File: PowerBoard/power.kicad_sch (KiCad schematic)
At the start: 1 part, among them U3 NCV1117DT33T5G

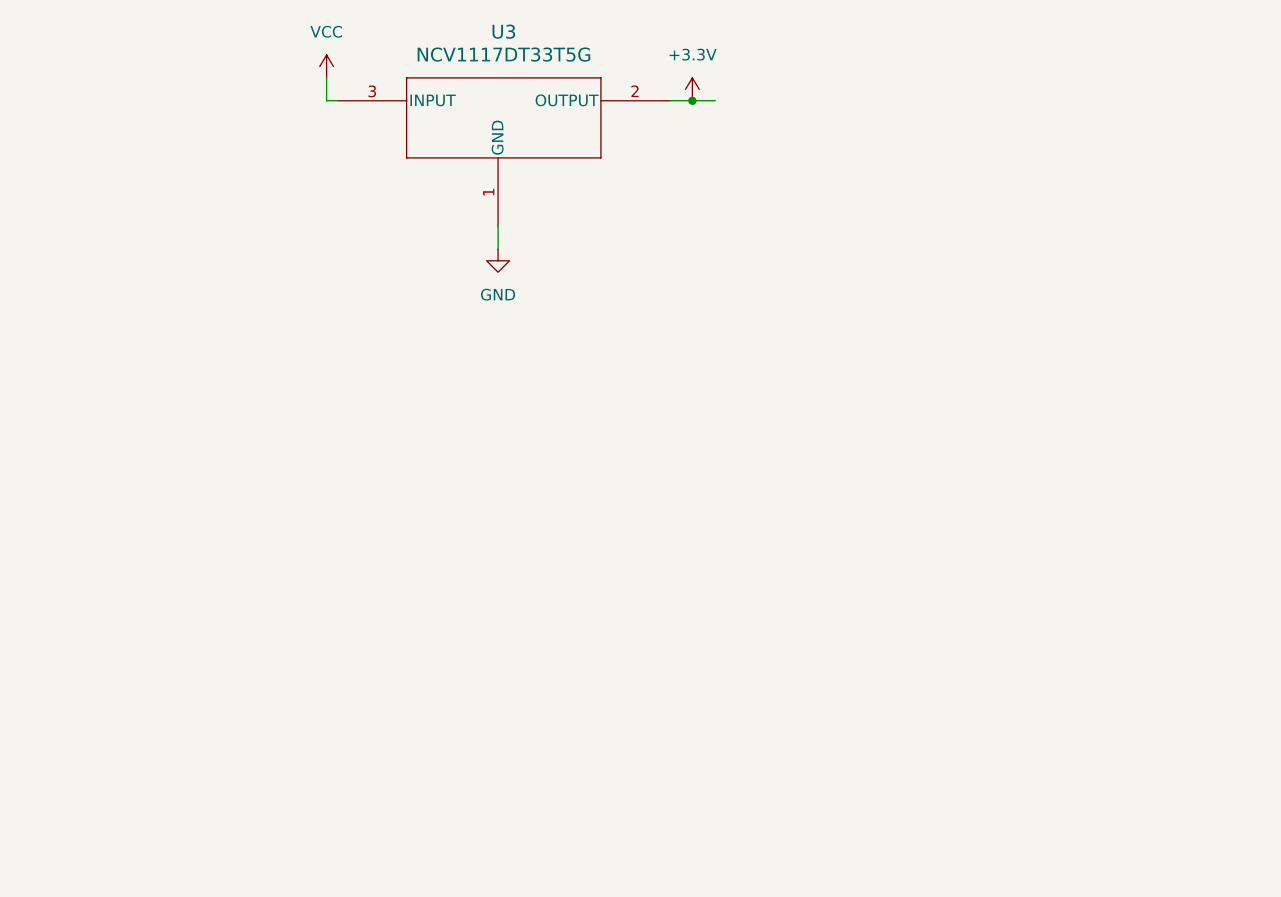
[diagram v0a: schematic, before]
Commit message: added 2040 flashing circuit and battery monitor
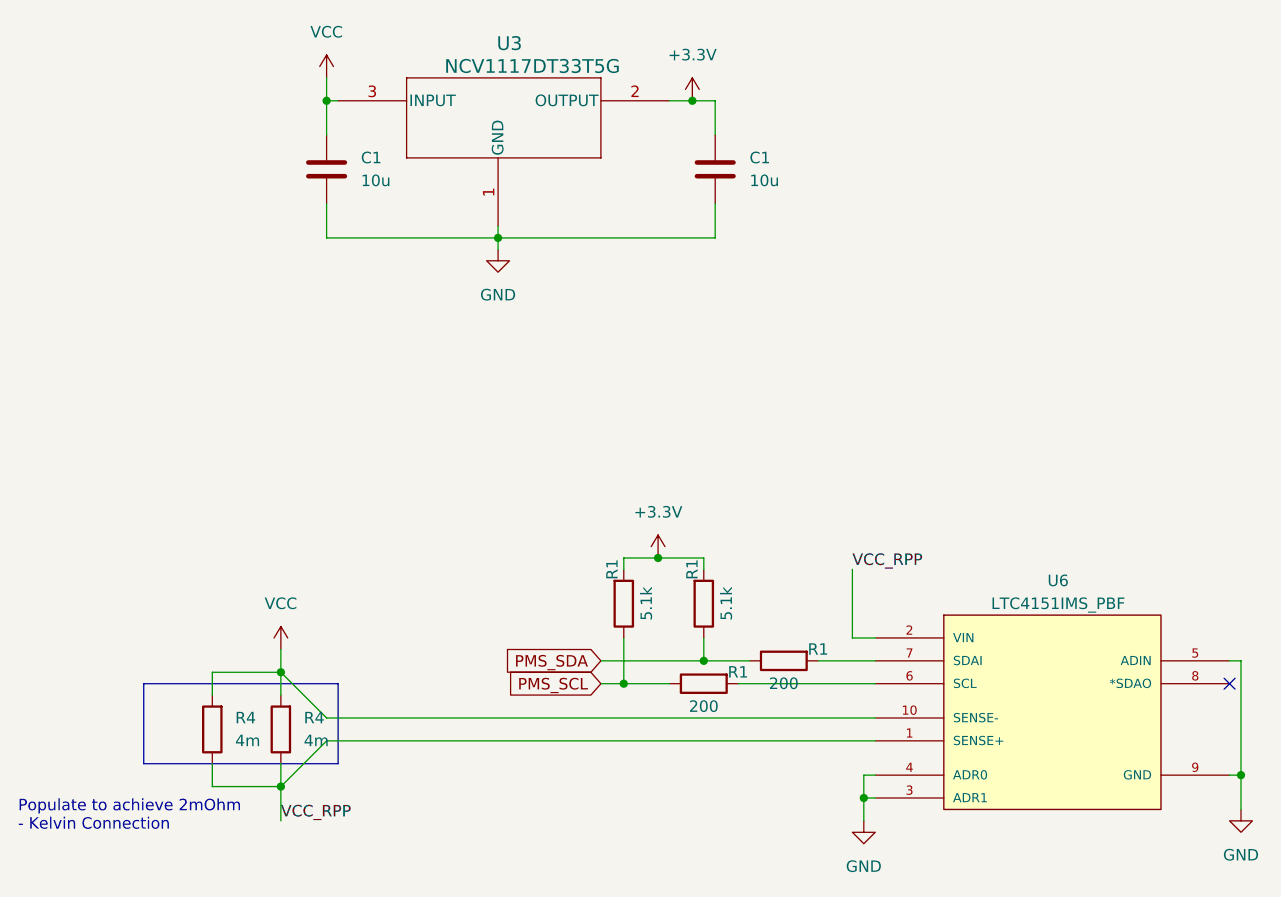
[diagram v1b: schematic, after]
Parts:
- added C1 (x2): 10u, Capacitor_SMD:C_0805_2012Metric, symbol Device:C
- added R1 (x2): 5.1k, Resistor_SMD:R_0603_1608Metric, symbol Device:R
- added R1 (x2): 200, Resistor_SMD:R_0603_1608Metric, symbol Device:R
- added R4 (x2): 4m, Resistor_SMD:R_1206_3216Metric, symbol Device:R
- added U6: LTC4151IMS_PBF, LTC4151IMS_PBF:MSOP-10_MS, symbol bots:LTC4151IMS_PBF
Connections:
- net +3.3V: now also C1.1, R1.2, R1.2
- net GND: now also C1.2, C1.2, U6.3 (ADR1), U6.4 (ADR0), U6.5 (ADIN), U6.9 (GND)
- net VCC: now also C1.1, R4.2, R4.2, U6.10 (SENSE-)
- new net: R1.2, U6.6 (SCL)
- new net: R1.2, U6.7 (SDAI)
- new net PMS_SCL: R1.1, R1.1
- new net PMS_SDA: R1.1, R1.1
- new net VCC_RPP: R4.1, R4.1, U6.1 (SENSE+), U6.2 (VIN)
- no-connect marks 0 -> 1
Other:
- note added: "Populate to achieve 2mOhm - Kelvin Connection"

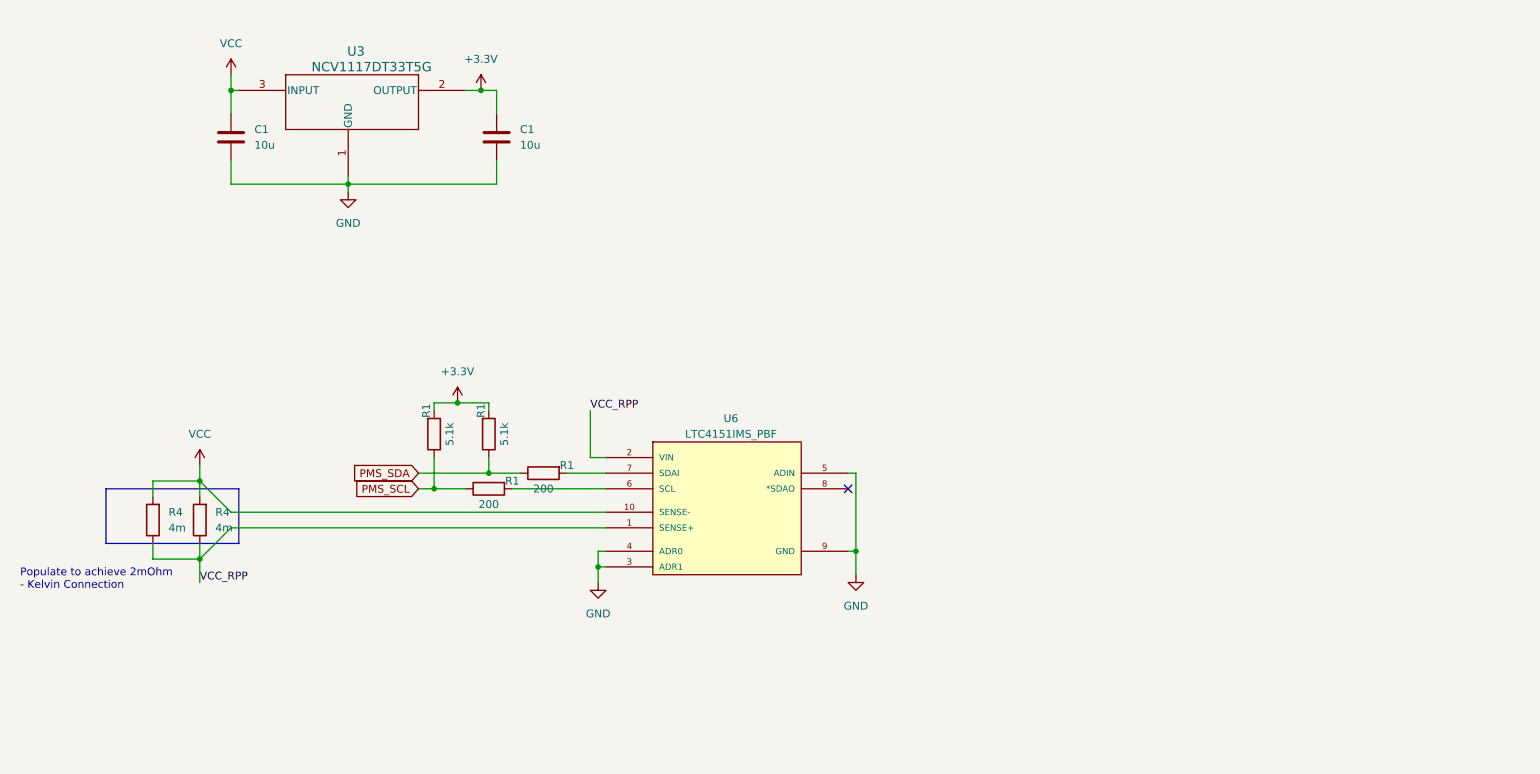
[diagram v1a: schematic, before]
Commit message: updated board shape + placed most components
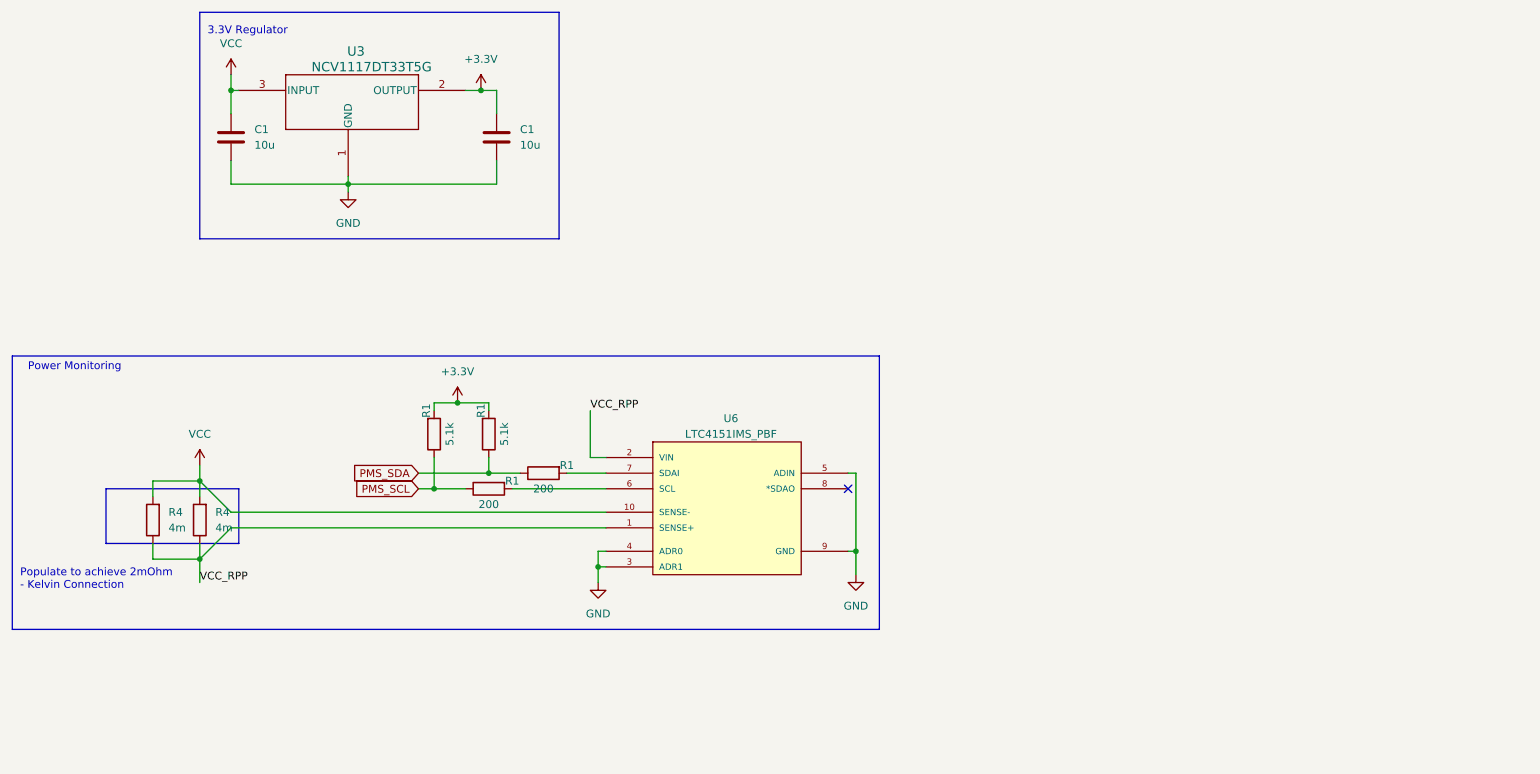
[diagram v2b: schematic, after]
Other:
- note added: "3.3V Regulator"
- note added: "Power Monitoring"
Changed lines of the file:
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@@
     (fill (type none))
+  )
+  (rectangle (start 24.13 77.47) (end 165.1 121.92)
+    (stroke (width 0) (type default))
+    (fill (type none))
+  )
+  (rectangle (start 54.61 21.59) (end 113.03 58.42)
+    (stroke (width 0) (type default))
+    (fill (type none))
+  )
+  (text "Power Monitoring" (at 26.67 80.01 0)
+    (effects (font (size 1.27 1.27)) (justify left bottom))
   )
   (text "Populate to achieve 2mOhm\n- Kelvin Connection" (at 25.4 115.57 0)
     (effects (font (size 1.27 1.27)) (justify left bottom))
   )
+  (text "3.3V Regulator" (at 55.88 25.4 0)
+    (effects (font (size 1.27 1.27)) (justify left bottom))
+  )

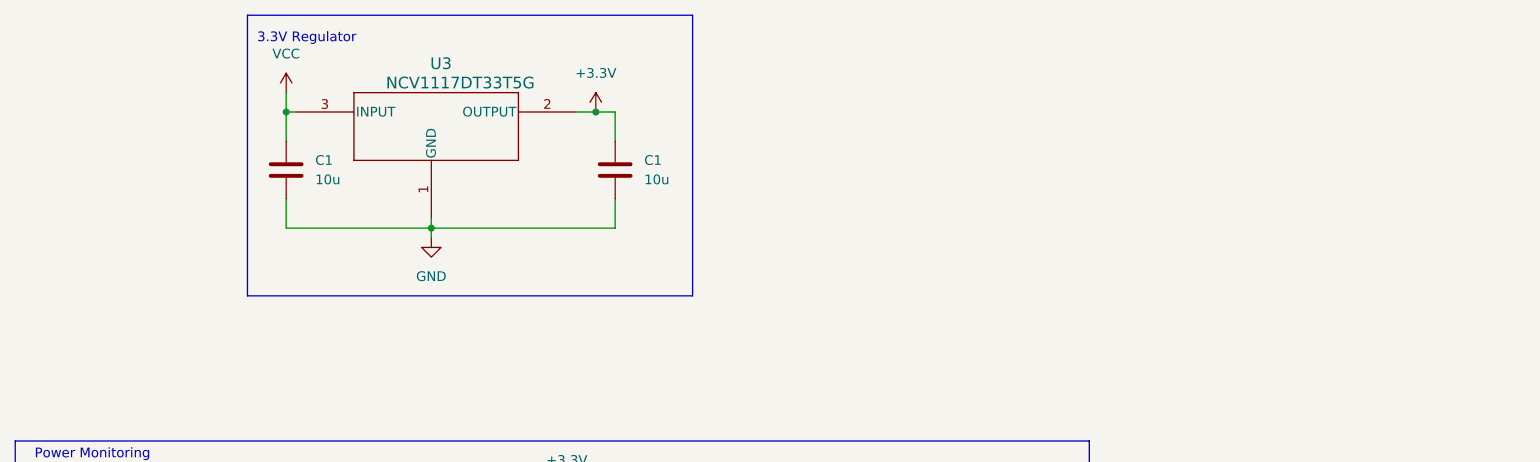
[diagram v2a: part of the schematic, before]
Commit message: board components mostly placed correctly
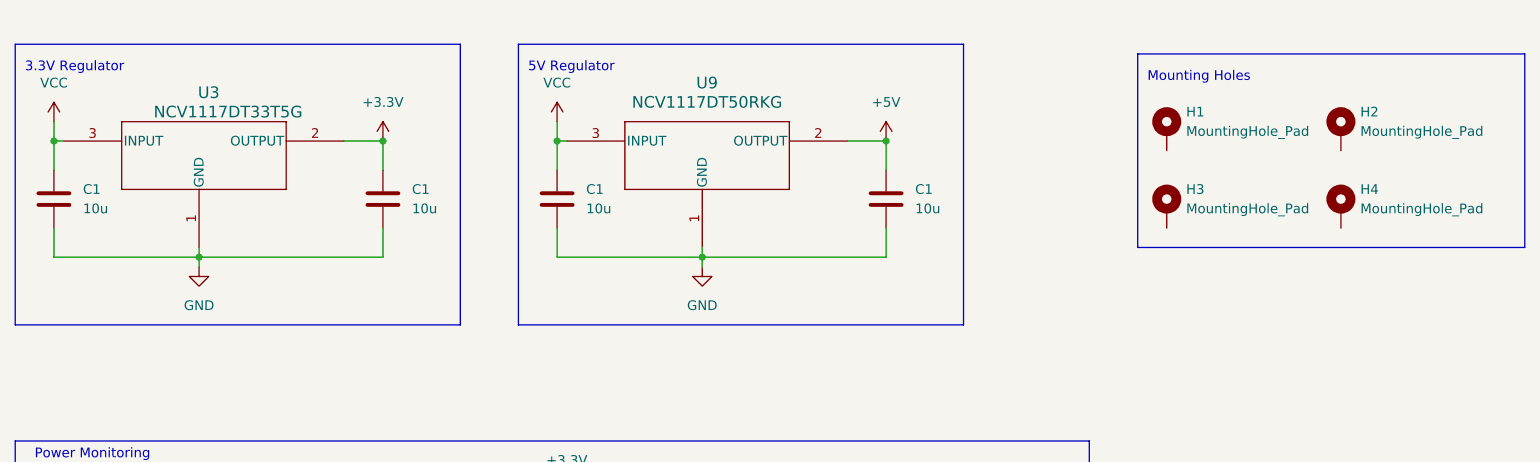
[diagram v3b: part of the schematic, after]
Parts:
- added C1 (x2): 10u, Capacitor_SMD:C_0805_2012Metric, symbol Device:C
- added H1, H2, H3, H4: MountingHole_Pad, MountingHole:MountingHole_2.7mm_M2.5_DIN965_Pad, symbol Mechanical:MountingHole_Pad
- added U9: NCV1117DT50RKG, bots:DPAK-3_ONS, symbol bots:NCV1117DT50RKG
- U3: footprint DPAK-3_ONS -> bots:DPAK-3_ONS
- U6: footprint LTC4151IMS_PBF:MSOP-10_MS -> bots:MSOP-10_MS
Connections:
- net GND: now also C1.2, C1.2, U9.1 (GND)
- net VCC: now also C1.1, U9.3 (INPUT)
- new net +5V: C1.1, U9.2 (OUTPUT)
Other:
- note added: "5V Regulator"
- note added: "Mounting Holes"
- moved on the sheet: C1, U3

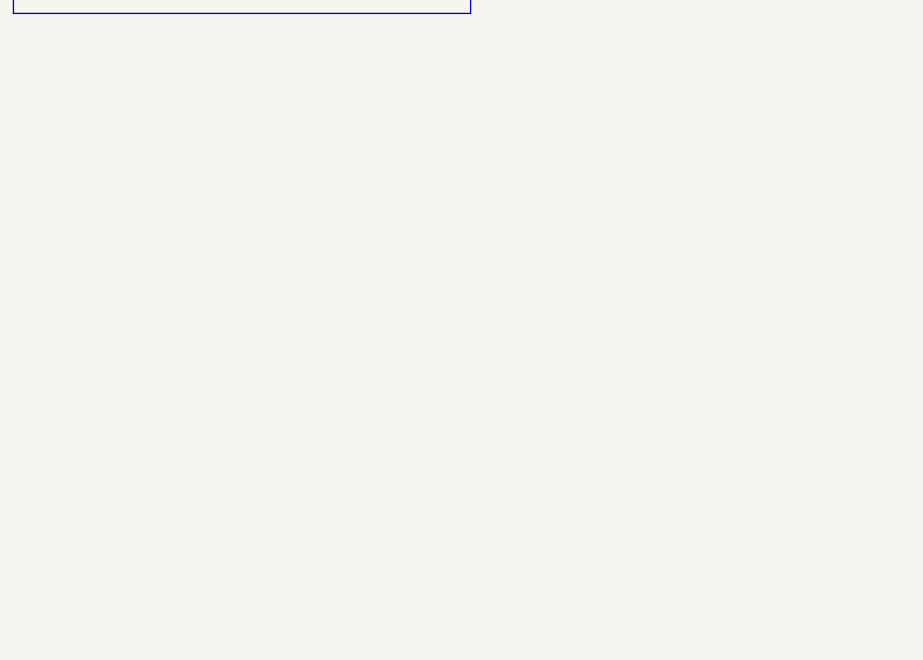
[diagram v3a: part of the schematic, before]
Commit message: updated small details + LEDS
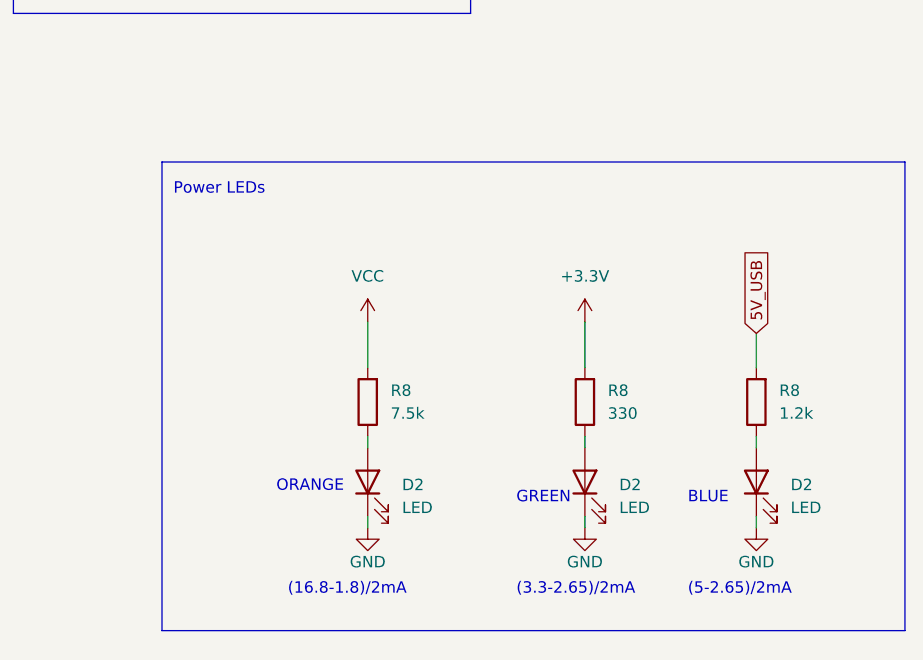
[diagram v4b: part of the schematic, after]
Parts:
- added D2 (x3): LED, LED_SMD:LED_1206_3216Metric, symbol Device:LED
- added R8: 1.2k, Resistor_SMD:R_0603_1608Metric, symbol Device:R
- added R8: 7.5k, Resistor_SMD:R_0603_1608Metric, symbol Device:R
- added R8: 330, Resistor_SMD:R_0603_1608Metric, symbol Device:R
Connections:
- net +3.3V: now also R8.2
- net GND: now also D2.1 (K), D2.1 (K), D2.1 (K)
- net VCC: now also R8.2
- new net: D2.2 (A), R8.1 (x3)
- new net 5V_USB: R8.2
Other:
- note added: "(16.8-1.8)/2mA"
- note added: "(3.3-2.65)/2mA"
- note added: "(5-2.65)/2mA"
- note added: "BLUE"
- note added: "GREEN"
- note added: "ORANGE"
- note added: "Power LEDs"

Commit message: update to layout
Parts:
- removed C1 (x2): 10u, Capacitor_SMD:C_0805_2012Metric, symbol Device:C
- removed U9: NCV1117DT50RKG, bots:DPAK-3_ONS, symbol bots:NCV1117DT50RKG
- added NT1: NetTie_2, NetTie:NetTie-2_SMD_Pad2.0mm, symbol bots:NetTie_2
- C1: footprint Capacitor_SMD:C_0805_2012Metric -> bots:C_0805_2012Metric
- D2: footprint LED_SMD:LED_1206_3216Metric -> bots:LED_1206_3216Metric
- R1, R8: footprint Resistor_SMD:R_0603_1608Metric -> bots:R_0603_1608Metric
- R4: footprint Resistor_SMD:R_1206_3216Metric -> bots:R_1206_3216Metric
- U6: footprint bots:MSOP-10_MS -> bots:MSOP-10_3x3mm_P0.5mm
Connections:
- net GND: now also NT1.2; no longer C1.2, U6.3 (ADR1), U6.4 (ADR0), U6.5 (ADIN), U6.9 (GND)
- net 3V3_DIO: now reaches D2.2 (A), R8.1
- net USB_DIO: now reaches D2.2 (A), R8.1
- net VCC_DIO: now reaches D2.2 (A), R8.1
- new net GNDPWR: C1.2, NT1.1, U6.3 (ADR1), U6.4 (ADR0), U6.5 (ADIN), U6.9 (GND)
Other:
- note removed: "5V Regulator"

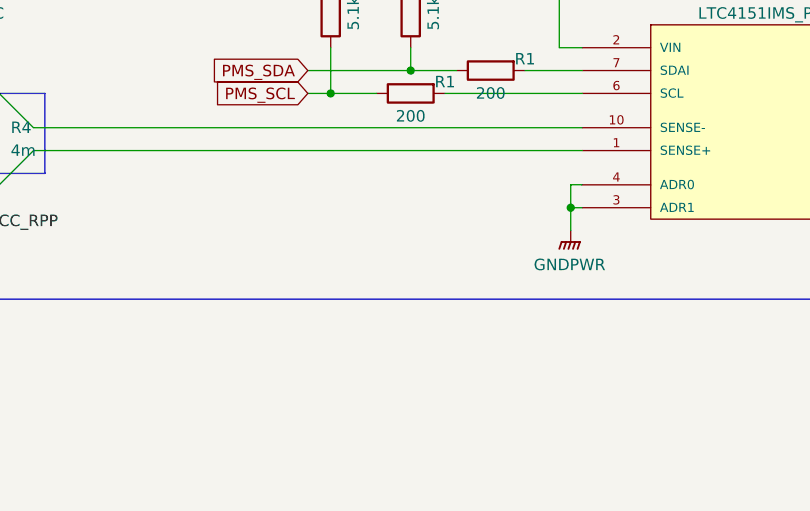
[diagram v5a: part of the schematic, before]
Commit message: layout v1 complete
- consider adding a auto discharge circuit
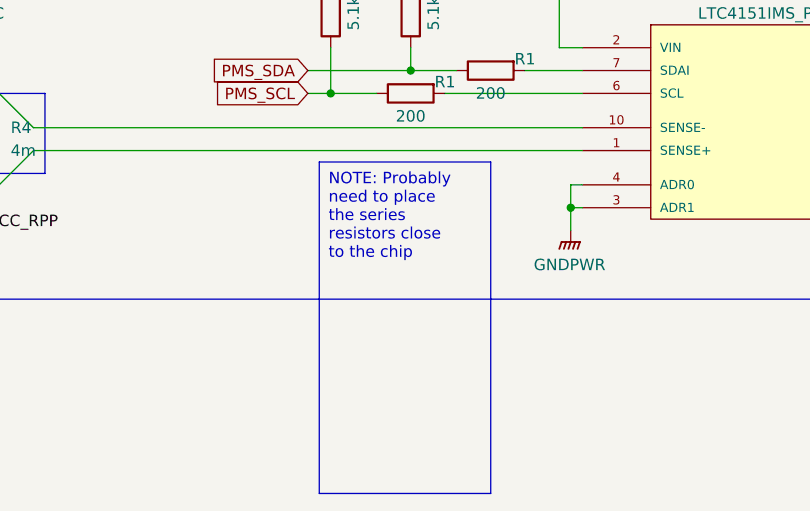
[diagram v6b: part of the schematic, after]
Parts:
- NT1: footprint NetTie:NetTie-2_SMD_Pad2.0mm -> bots:NetTie-2_SMD_Pad2.0mm
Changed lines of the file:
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@@
     (fill (type none))
+  )
+  (text_box "NOTE: Probably need to place the series resistors close to the chip"
+    (at 91.44 106.68 0) (size 19.05 36.83)
+    (stroke (width 0) (type default) (color 255 0 17 1))
+    (fill (type color) (color 57 255 0 1))
+    (effects (font (size 1.27 1.27)) (justify left top))
   )
   (text "Power Monitoring" (at 26.67 80.01 0)
@@
       (effects (font (size 1.27 1.27)))
     )
-    (property "Footprint" "NetTie:NetTie-2_SMD_Pad2.0mm" (at 39.37 53.34 0)
-      (effects (font (size 1.27 1.27)) hide)
-    )
+    (property "Footprint" "bots:NetTie-2_SMD_Pad2.0mm" (at 39.37 53.34 0)
+      (effects (font (size 1.27 1.27)) hide)
+    )
